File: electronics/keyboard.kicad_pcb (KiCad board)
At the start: 2 copper layers, 181 parts, among them J1 CONN_02X10, SW1 SW_Push, SW10 SW_Push, SW11 SW_Push, SW12 SW_Push, SW13 SW_Push, SW14 SW_Push, SW15 SW_Push, SW16 SW_Push, SW17 SW_Push, SW18 SW_Push, SW19 SW_Push, SW2 SW_Push, SW20 SW_Push, SW21 SW_Push, SW22 SW_Push, SW23 SW_Push, SW24 SW_Push, SW25 SW_Push, SW26 SW_Push, SW27 SW_Push, SW28 SW_Push, SW29 SW_Push, SW3 SW_Push, SW30 SW_Push, SW31 SW_Push, SW32 SW_Push, SW33 SW_Push, SW34 SW_Push, SW35 SW_Push, SW36 SW_Push, SW37 SW_Push, SW38 SW_Push, SW39 SW_Push, SW4 SW_Push, SW40 SW_Push, SW41 SW_Push, SW42 SW_Push, SW43 SW_Push, SW44 SW_Push, SW45 SW_Push, SW46 SW_Push, SW47 SW_Push, SW48 SW_Push, SW49 SW_Push, SW5 SW_Push, SW50 SW_Push, SW51 SW_Push, SW52 SW_Push, SW53 SW_Push, SW54 SW_Push, SW55 SW_Push, SW56 SW_Push, SW57 SW_Push, SW58 SW_Push, SW59 SW_Push, SW6 SW_Push, SW60 SW_Push, SW61 SW_Push, SW62 SW_Push, SW63 SW_Push, SW64 SW_Push, SW65 SW_Push, SW66 SW_Push, SW67 SW_Push, SW68 SW_Push, SW69 SW_Push, SW7 SW_Push, SW70 SW_Push, SW71 SW_Push, SW72 SW_Push, SW73 SW_Push, SW74 SW_Push, SW75 SW_Push, SW76 SW_Push, SW77 SW_Push, SW78 SW_Push, SW79 SW_Push, SW8 SW_Push, SW80 SW_Push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

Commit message: routed the 2nd column
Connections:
- SW15 pad 2: Net-(SW15-Pad2) -> /PB1
- SW23 pad 2: Net-(SW23-Pad2) -> /PB1
- SW44 pad 2: Net-(SW44-Pad2) -> /PB1
- SW47 pad 2: Net-(SW47-Pad2) -> /PB1
- SW53 pad 2: Net-(SW53-Pad2) -> /PB1
- SW71 pad 2: Net-(SW71-Pad2) -> /PB1
- SW73 pad 2: Net-(SW73-Pad2) -> /PB1
- SW75 pad 2: Net-(SW75-Pad2) -> /PB1
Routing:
- net /PB1: track 0.00 -> 323.7 mm

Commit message: Added two columns
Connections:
- SW17 pad 2: Net-(SW17-Pad2) -> /PB3
- SW18 pad 2: Net-(SW18-Pad2) -> /PB3
- SW20 pad 2: Net-(SW20-Pad2) -> /PB2
- SW28 pad 2: Net-(SW28-Pad2) -> /PB2
- SW31 pad 2: Net-(SW31-Pad2) -> /PB2
- SW33 pad 2: Net-(SW33-Pad2) -> /PB3
- SW34 pad 2: Net-(SW34-Pad2) -> /PB2
- SW35 pad 2: Net-(SW35-Pad2) -> /PB3
- SW39 pad 2: Net-(SW39-Pad2) -> /PB2
- SW40 pad 2: Net-(SW40-Pad2) -> /PB3
- SW41 pad 2: Net-(SW41-Pad2) -> /PB2
- SW45 pad 2: Net-(SW45-Pad2) -> /PB3
- SW46 pad 2: Net-(SW46-Pad2) -> /PB2
- SW5 pad 2: Net-(SW5-Pad2) -> /PB3
- SW78 pad 2: Net-(SW78-Pad2) -> /PB2
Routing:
- net /PB2: track 0.00 -> 355.2 mm
- net /PB3: track 0.00 -> 288.1 mm

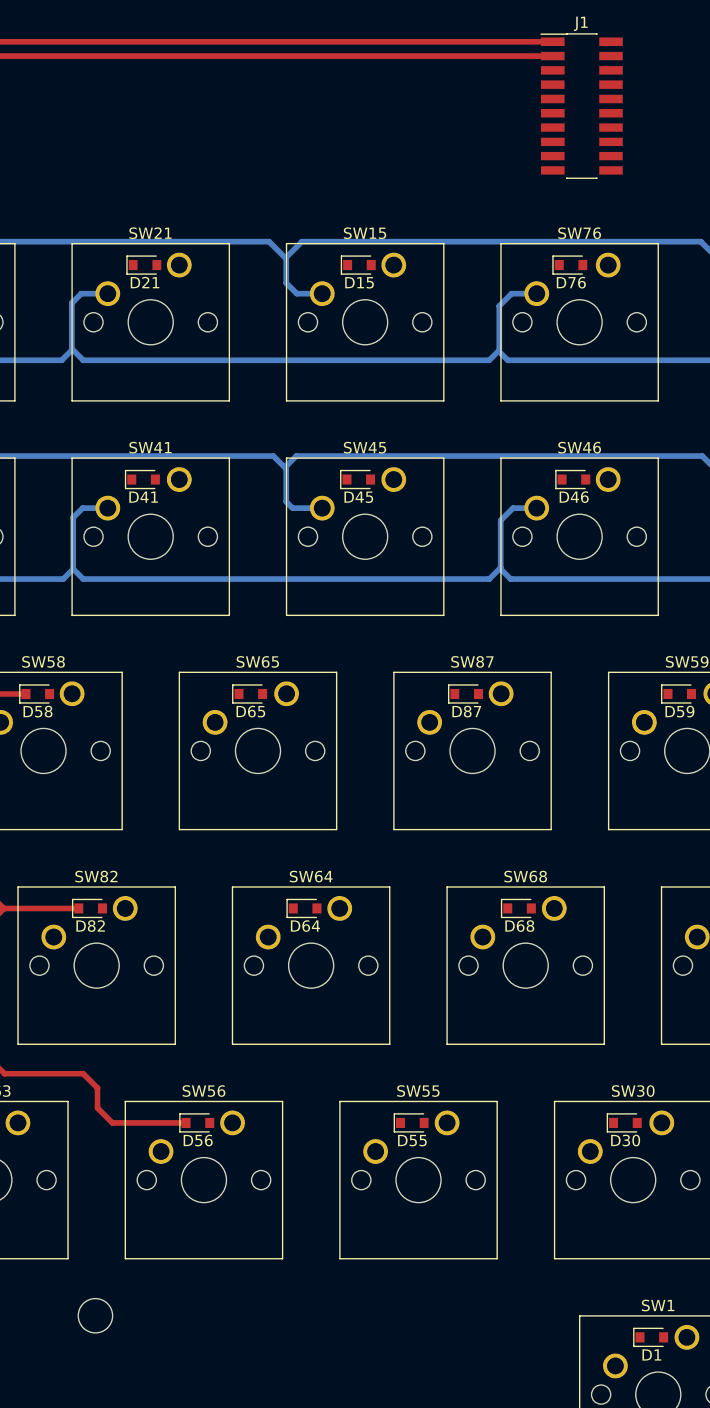
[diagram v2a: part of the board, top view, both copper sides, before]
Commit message: Worked further on the layout
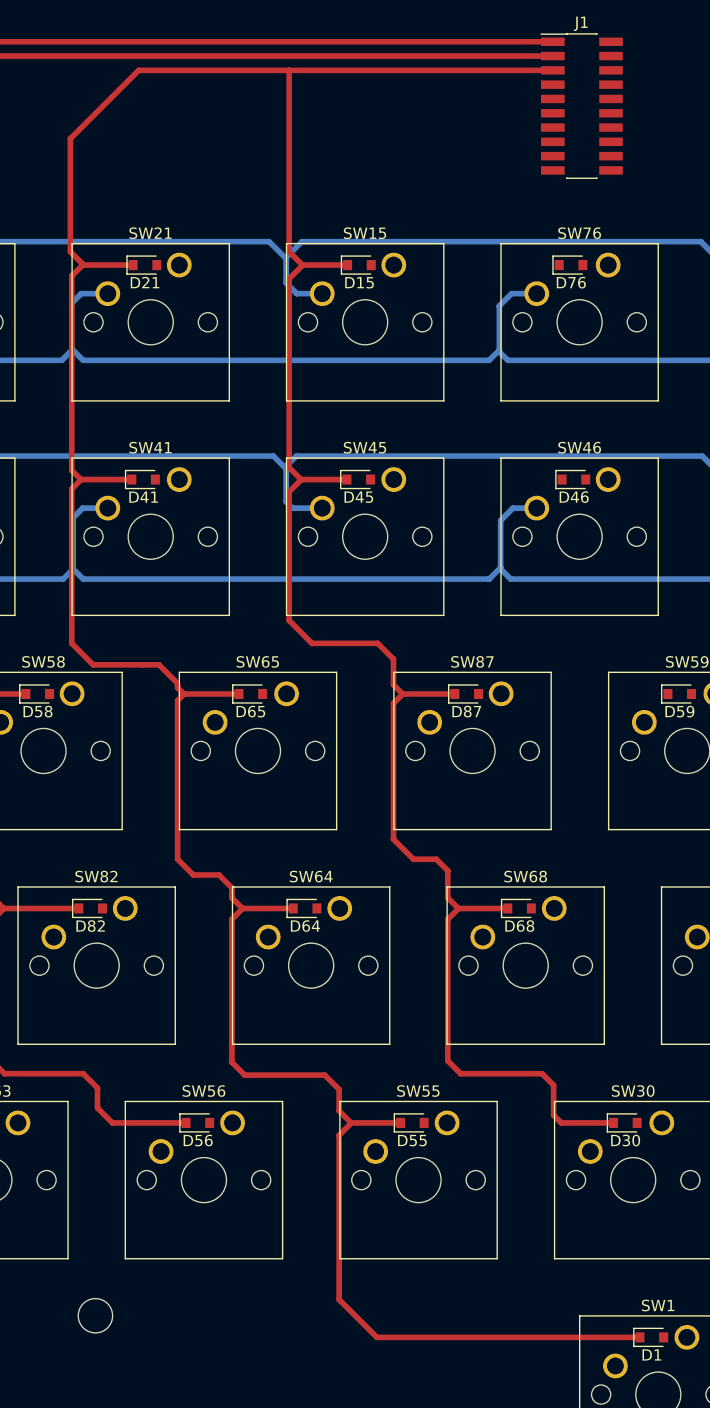
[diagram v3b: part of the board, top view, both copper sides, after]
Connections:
- D1 pad 1: Net-(D1-Pad1) -> /PA2
- D15 pad 1: Net-(D15-Pad1) -> /PA2
- D21 pad 1: Net-(D21-Pad1) -> /PA2
- D30 pad 1: Net-(D30-Pad1) -> /PA2
- D41 pad 1: Net-(D41-Pad1) -> /PA2
- D45 pad 1: Net-(D45-Pad1) -> /PA2
- D55 pad 1: Net-(D55-Pad1) -> /PA2
- D64 pad 1: Net-(D64-Pad1) -> /PA2
- D65 pad 1: Net-(D65-Pad1) -> /PA2
- D68 pad 1: Net-(D68-Pad1) -> /PA2
- D87 pad 1: Net-(D87-Pad1) -> /PA2
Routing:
- net /PA2: track 0.00 -> 359.6 mm

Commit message: more layout
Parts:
- moved J1 49.9 mm to (200.0, 100.2)
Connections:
- D18 pad 1: Net-(D18-Pad1) -> /PA3
- D24 pad 1: Net-(D24-Pad1) -> /PA3
- D46 pad 1: Net-(D46-Pad1) -> /PA3
- D48 pad 1: Net-(D48-Pad1) -> /PA3
- D54 pad 1: Net-(D54-Pad1) -> /PA3
- D59 pad 1: Net-(D59-Pad1) -> /PA3
- D61 pad 1: Net-(D61-Pad1) -> /PA3
- D67 pad 1: Net-(D67-Pad1) -> /PA3
- D75 pad 1: Net-(D75-Pad1) -> /PA3
- D76 pad 1: Net-(D76-Pad1) -> /PA3
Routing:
- net /PA3: track 0.00 -> 328.1 mm
- net /PA2: track 359.6 -> 409.7 mm
- net /PA0: track 494.8 -> 544.7 mm
- net /PA1: track 415.8 -> 465.7 mm

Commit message: worked further on interconnect
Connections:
- SW13 pad 2: Net-(SW13-Pad2) -> /PB4
- SW16 pad 2: Net-(SW16-Pad2) -> /PB4
- SW22 pad 2: Net-(SW22-Pad2) -> /PB4
- SW25 pad 2: Net-(SW25-Pad2) -> /PB5
- SW51 pad 2: Net-(SW51-Pad2) -> /PB4
- SW58 pad 2: Net-(SW58-Pad2) -> /PB5
- SW59 pad 2: Net-(SW59-Pad2) -> /PB4
- SW60 pad 2: Net-(SW60-Pad2) -> /PB5
- SW61 pad 2: Net-(SW61-Pad2) -> /PB5
- SW62 pad 2: Net-(SW62-Pad2) -> /PB4
- SW65 pad 2: Net-(SW65-Pad2) -> /PB4
- SW69 pad 2: Net-(SW69-Pad2) -> /PB5
- SW8 pad 2: Net-(SW8-Pad2) -> /PB5
- SW87 pad 2: Net-(SW87-Pad2) -> /PB5
- SW9 pad 2: Net-(SW9-Pad2) -> /PB4
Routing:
- net /PB4: track 0.00 -> 353.2 mm
- net /PB5: track 0.00 -> 286.5 mm

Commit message: Further work on interconnect
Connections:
- D31 pad 1: Net-(D31-Pad1) -> /PA4
- D33 pad 1: Net-(D33-Pad1) -> /PA4
- D42 pad 1: Net-(D42-Pad1) -> /PA4
- D44 pad 1: Net-(D44-Pad1) -> /PA4
- D51 pad 1: Net-(D51-Pad1) -> /PA4
- D52 pad 1: Net-(D52-Pad1) -> /PA4
- D69 pad 1: Net-(D69-Pad1) -> /PA4
- D74 pad 1: Net-(D74-Pad1) -> /PA4
- D81 pad 1: Net-(D81-Pad1) -> /PA4
- D83 pad 1: Net-(D83-Pad1) -> /PA4
- D90 pad 1: Net-(D90-Pad1) -> /PA4
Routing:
- net /PA4: track 0.00 -> 326.1 mm

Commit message: Another ROW layouted
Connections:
- D27 pad 1: Net-(D27-Pad1) -> /PA5
- D34 pad 1: Net-(D34-Pad1) -> /PA5
- D35 pad 1: Net-(D35-Pad1) -> /PA5
- D36 pad 1: Net-(D36-Pad1) -> /PA5
- D43 pad 1: Net-(D43-Pad1) -> /PA5
- D47 pad 1: Net-(D47-Pad1) -> /PA5
- D50 pad 1: Net-(D50-Pad1) -> /PA5
- D6 pad 1: Net-(D6-Pad1) -> /PA5
- D60 pad 1: Net-(D60-Pad1) -> /PA5
- D62 pad 1: Net-(D62-Pad1) -> /PA5
- D66 pad 1: Net-(D66-Pad1) -> /PA5
- D85 pad 1: Net-(D85-Pad1) -> /PA5
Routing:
- net /PA5: track 0.00 -> 387.5 mm

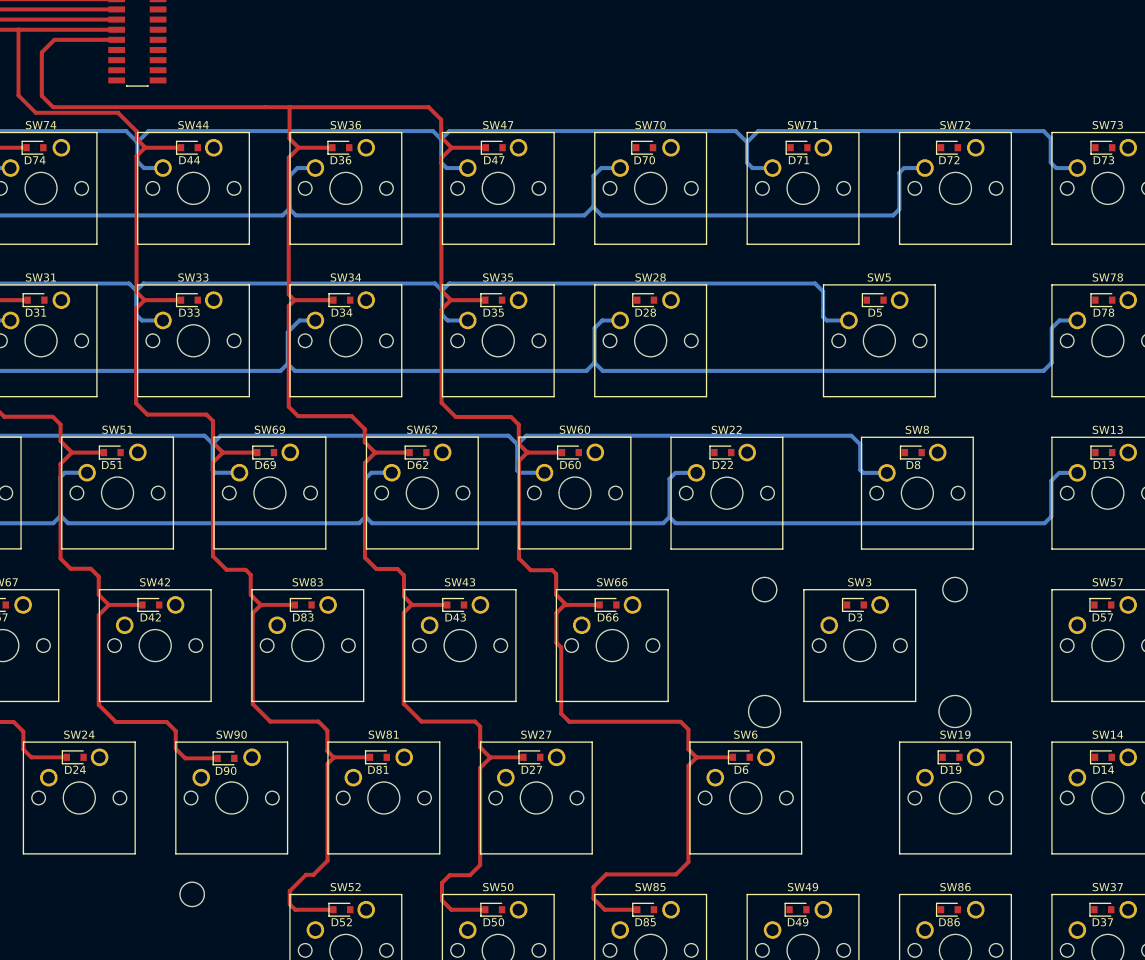
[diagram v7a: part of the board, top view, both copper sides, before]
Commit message: Finished Row layout
Todo:
    - Route the last columns
    - change some layers in the layout (diodes, connector)
    - add fill
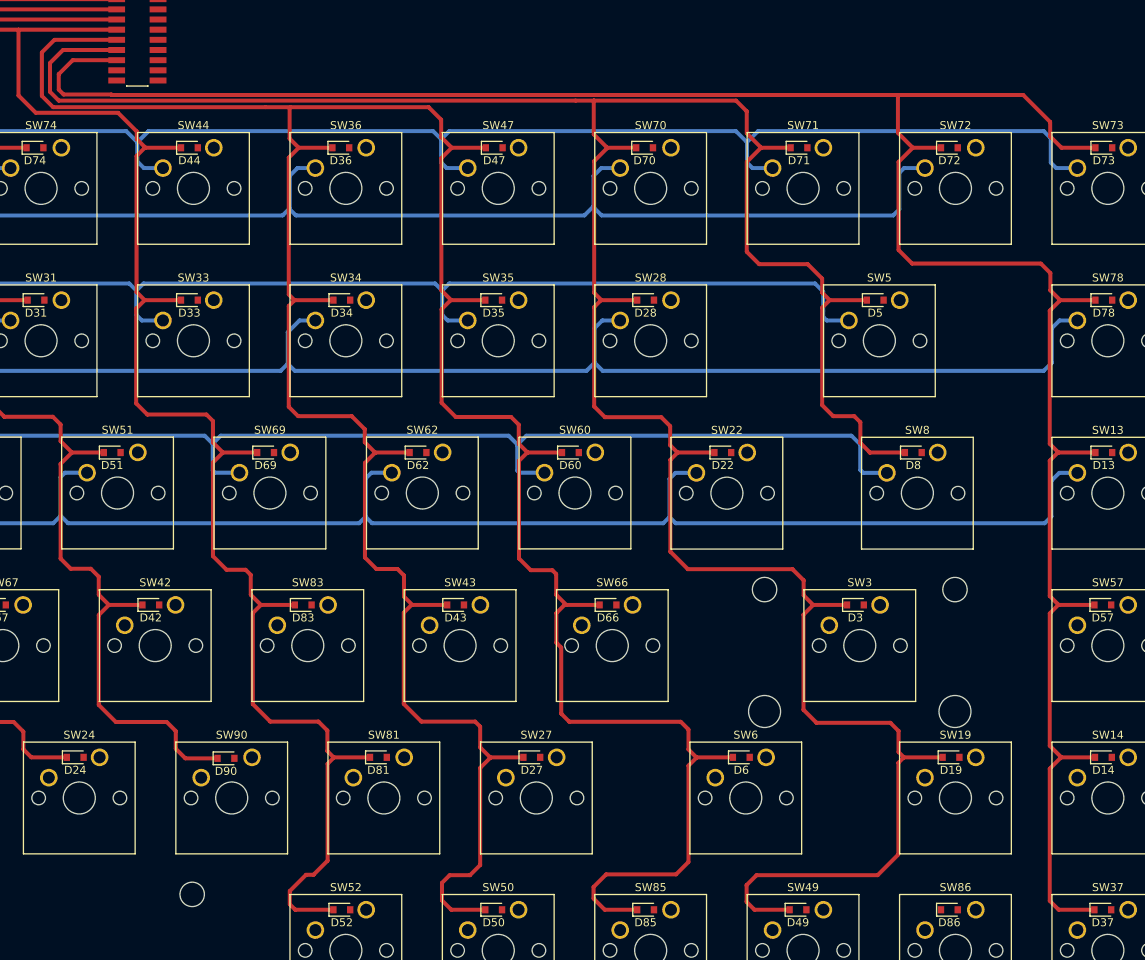
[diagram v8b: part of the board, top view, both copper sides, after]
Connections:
- D13 pad 1: Net-(D13-Pad1) -> /PA7
- D14 pad 1: Net-(D14-Pad1) -> /PA7
- D19 pad 1: Net-(D19-Pad1) -> /PA6
- D22 pad 1: Net-(D22-Pad1) -> /PA6
- D28 pad 1: Net-(D28-Pad1) -> /PA6
- D3 pad 1: Net-(D3-Pad1) -> /PA6
- D37 pad 1: Net-(D37-Pad1) -> /PA7
- D49 pad 1: Net-(D49-Pad1) -> /PA6
- D5 pad 1: Net-(D5-Pad1) -> /PA6
- D57 pad 1: Net-(D57-Pad1) -> /PA7
- D70 pad 1: Net-(D70-Pad1) -> /PA6
- D71 pad 1: Net-(D71-Pad1) -> /PA6
- D72 pad 1: Net-(D72-Pad1) -> /PA7
- D73 pad 1: Net-(D73-Pad1) -> /PA7
- D78 pad 1: Net-(D78-Pad1) -> /PA7
- D8 pad 1: Net-(D8-Pad1) -> /PA6
- D86 pad 1: Net-(D86-Pad1) -> /PA7
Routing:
- net /PA6: track 0.00 -> 351.7 mm
- net /PA7: track 0.00 -> 294.5 mm
